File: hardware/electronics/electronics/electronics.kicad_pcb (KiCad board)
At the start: 2 copper layers, 130 x 100 mm, 14 parts, among them J1 Conn_Coaxial_Small, M1 Parachute_Servo, M2 Parachute_Servo, Q1 BC547, SW1 RBF, U1 RFM95W-915S2, U2 BMP585, U3 LSM6DS3, U4 SD Card mini module, U5 ESP32-S3-DEVKITC-1-N8R2, U6 GPS M8N, U7 MINI 560 STEP DOWN

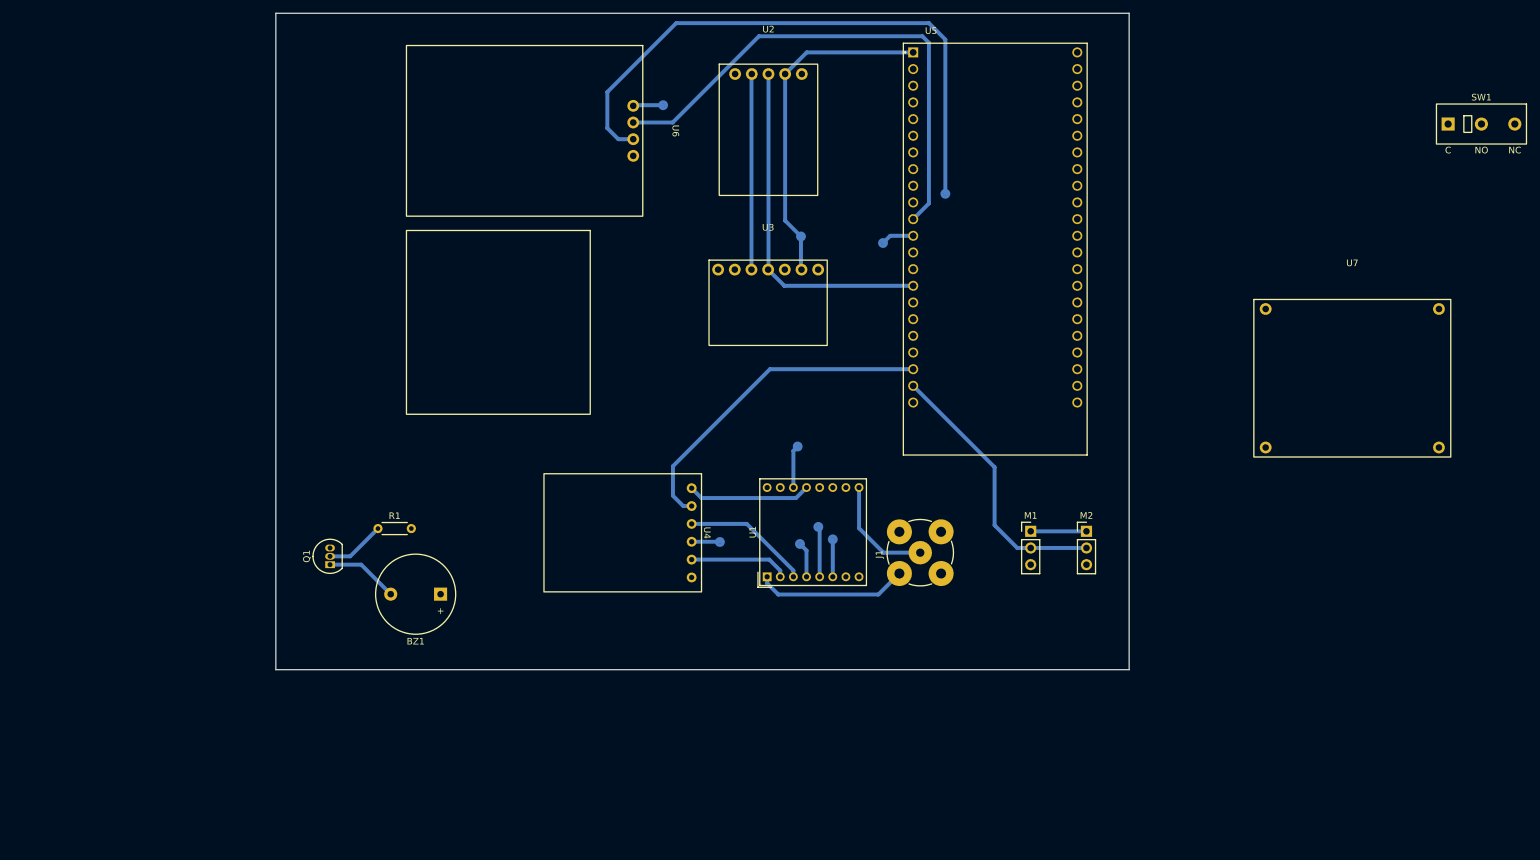
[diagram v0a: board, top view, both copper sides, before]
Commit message: Update flight-computer hardware files (PCB)
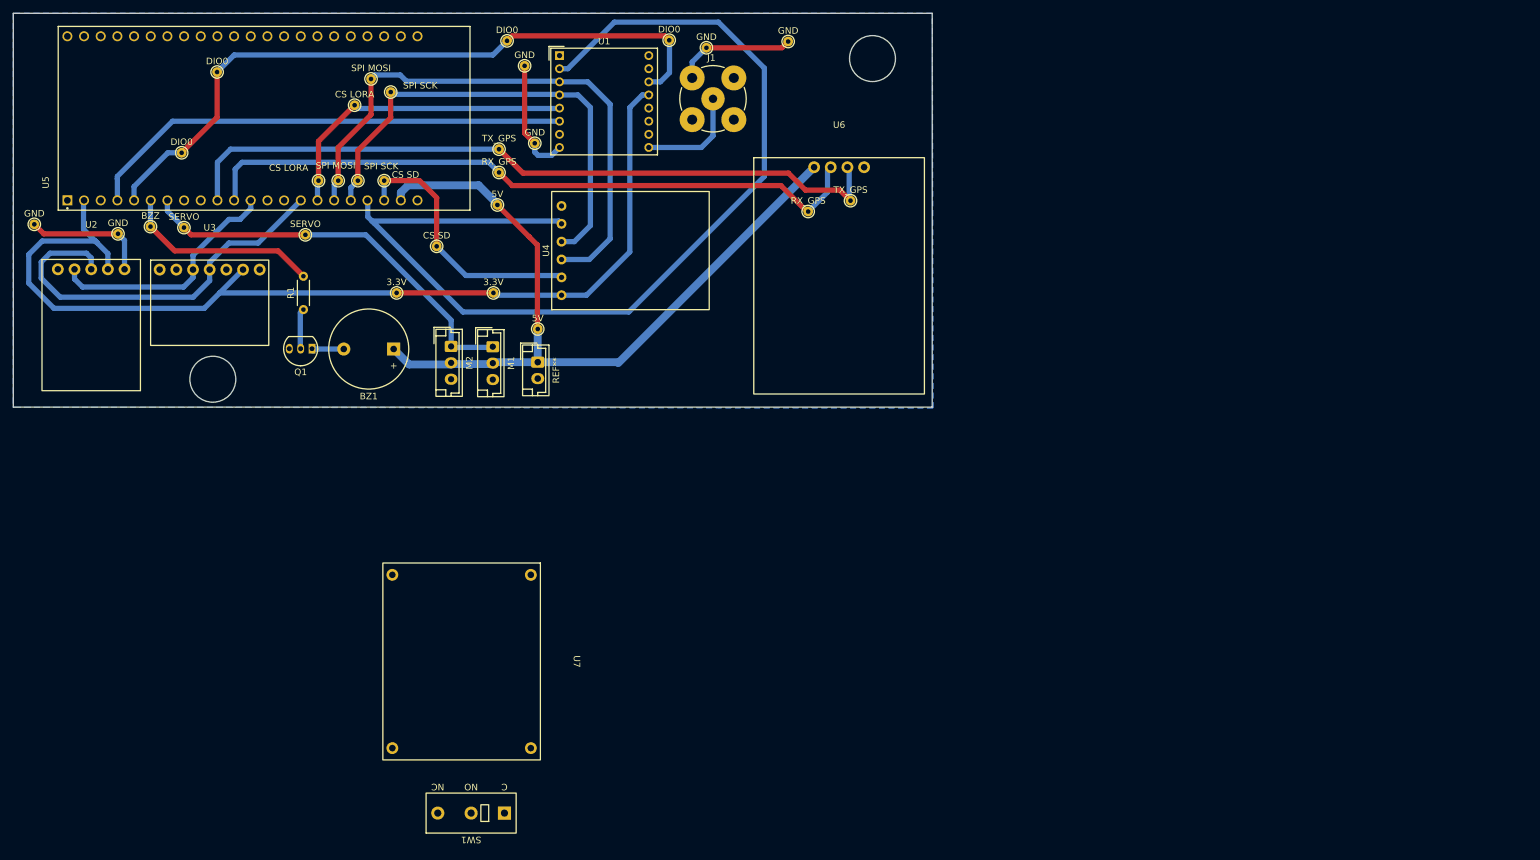
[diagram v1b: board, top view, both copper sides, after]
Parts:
- added 3.3V: TestPoint_THTPad_D1.5mm_Drill0.7mm, TestPoint:TestPoint_THTPad_D1.5mm_Drill0.7mm, F.Cu at (103.4, 92.6)
- added 3.3V: TestPoint_THTPad_D1.5mm_Drill0.7mm, TestPoint:TestPoint_THTPad_D1.5mm_Drill0.7mm, F.Cu at (118.2, 92.6)
- added 5V: TestPoint_THTPad_D1.5mm_Drill0.7mm, TestPoint:TestPoint_THTPad_D1.5mm_Drill0.7mm, F.Cu at (124.9, 98.1)
- added 5V: TestPoint_THTPad_D1.5mm_Drill0.7mm, TestPoint:TestPoint_THTPad_D1.5mm_Drill0.7mm, F.Cu at (118.8, 79.2)
- added BZZ: TestPoint_THTPad_D1.5mm_Drill0.7mm, TestPoint:TestPoint_THTPad_D1.5mm_Drill0.7mm, F.Cu at (65.9, 82.5)
- added CS LORA: TestPoint_THTPad_D1.5mm_Drill0.7mm, TestPoint:TestPoint_THTPad_D1.5mm_Drill0.7mm, F.Cu at (91.5, 75.5)
- added CS LORA: TestPoint_THTPad_D1.5mm_Drill0.7mm, TestPoint:TestPoint_THTPad_D1.5mm_Drill0.7mm, F.Cu at (97.0, 64.0)
- added CS SD: TestPoint_THTPad_D1.5mm_Drill0.7mm, TestPoint:TestPoint_THTPad_D1.5mm_Drill0.7mm, F.Cu at (101.5, 75.5)
- added CS SD: TestPoint_THTPad_D1.5mm_Drill0.7mm, TestPoint:TestPoint_THTPad_D1.5mm_Drill0.7mm, F.Cu at (109.5, 85.5)
- added DIO0: TestPoint_THTPad_D1.5mm_Drill0.7mm, TestPoint:TestPoint_THTPad_D1.5mm_Drill0.7mm, F.Cu at (76.0, 59.0)
- added DIO0: TestPoint_THTPad_D1.5mm_Drill0.7mm, TestPoint:TestPoint_THTPad_D1.5mm_Drill0.7mm, F.Cu at (120.2, 54.2)
- added DIO0: TestPoint_THTPad_D1.5mm_Drill0.7mm, TestPoint:TestPoint_THTPad_D1.5mm_Drill0.7mm, F.Cu at (70.7, 71.2)
- added DIO0: TestPoint_THTPad_D1.5mm_Drill0.7mm, TestPoint:TestPoint_THTPad_D1.5mm_Drill0.7mm, F.Cu at (144.9, 54.1)
- added GND: TestPoint_THTPad_D1.5mm_Drill0.7mm, TestPoint:TestPoint_THTPad_D1.5mm_Drill0.7mm, F.Cu at (163.1, 54.3)
- added GND: TestPoint_THTPad_D1.5mm_Drill0.7mm, TestPoint:TestPoint_THTPad_D1.5mm_Drill0.7mm, F.Cu at (124.5, 69.8)
- added GND: TestPoint_THTPad_D1.5mm_Drill0.7mm, TestPoint:TestPoint_THTPad_D1.5mm_Drill0.7mm, F.Cu at (61.0, 83.6)
- added GND: TestPoint_THTPad_D1.5mm_Drill0.7mm, TestPoint:TestPoint_THTPad_D1.5mm_Drill0.7mm, F.Cu at (122.9, 58.0)
- added GND: TestPoint_THTPad_D1.5mm_Drill0.7mm, TestPoint:TestPoint_THTPad_D1.5mm_Drill0.7mm, F.Cu at (150.6, 55.2)
- added GND: TestPoint_THTPad_D1.5mm_Drill0.7mm, TestPoint:TestPoint_THTPad_D1.5mm_Drill0.7mm, F.Cu at (48.2, 82.2)
- added REF**: JST_EH_B2B-EH-A_1x02_P2.50mm_Vertical, Connector_JST:JST_EH_B2B-EH-A_1x02_P2.50mm_Vertical, F.Cu at (124.9, 103.2)
- added RX_GPS: TestPoint_THTPad_D1.5mm_Drill0.7mm, TestPoint:TestPoint_THTPad_D1.5mm_Drill0.7mm, F.Cu at (166.1, 80.2)
- added RX_GPS: TestPoint_THTPad_D1.5mm_Drill0.7mm, TestPoint:TestPoint_THTPad_D1.5mm_Drill0.7mm, F.Cu at (119.0, 74.2)
- added SERVO: TestPoint_THTPad_D1.5mm_Drill0.7mm, TestPoint:TestPoint_THTPad_D1.5mm_Drill0.7mm, F.Cu at (71.0, 82.7)
- added SERVO: TestPoint_THTPad_D1.5mm_Drill0.7mm, TestPoint:TestPoint_THTPad_D1.5mm_Drill0.7mm, F.Cu at (89.5, 83.8)
- added SPI MOSI: TestPoint_THTPad_D1.5mm_Drill0.7mm, TestPoint:TestPoint_THTPad_D1.5mm_Drill0.7mm, F.Cu at (94.5, 75.5)
- added SPI MOSI: TestPoint_THTPad_D1.5mm_Drill0.7mm, TestPoint:TestPoint_THTPad_D1.5mm_Drill0.7mm, F.Cu at (99.5, 60.0)
- added SPI SCK: TestPoint_THTPad_D1.5mm_Drill0.7mm, TestPoint:TestPoint_THTPad_D1.5mm_Drill0.7mm, F.Cu at (97.5, 75.5)
- added SPI SCK: TestPoint_THTPad_D1.5mm_Drill0.7mm, TestPoint:TestPoint_THTPad_D1.5mm_Drill0.7mm, F.Cu at (102.5, 62.0)
- added TX_GPS: TestPoint_THTPad_D1.5mm_Drill0.7mm, TestPoint:TestPoint_THTPad_D1.5mm_Drill0.7mm, F.Cu at (172.6, 78.5)
- added TX_GPS: TestPoint_THTPad_D1.5mm_Drill0.7mm, TestPoint:TestPoint_THTPad_D1.5mm_Drill0.7mm, F.Cu at (119.0, 70.7)
- M1, M2: footprint Connector_PinHeader_2.54mm:PinHeader_1x03_P2.54mm_Vertical -> Connector_JST:JST_EH_B3B-EH-A_1x03_P2.50mm_Vertical
- moved SW1 178.0 mm to (119.8, 171.8), turned to 180 degrees
- moved U7 135.4 mm to (125.3, 148.8), turned to -90 degrees
- moved U5 113.2 mm to (83.2, 66.0), turned to 90 degrees
- moved U2 107.4 mm to (56.9, 87.5)
- moved M2 100.8 mm to (111.7, 100.8), turned to -90 degrees
- moved M1 86.6 mm to (118.0, 100.8), turned to -90 degrees
- moved U1 85.5 mm to (128.2, 56.4), turned to 0 degrees
- moved U3 85.1 mm to (74.9, 87.6)
- moved J1 76.0 mm to (151.6, 63.0), turned to 0 degrees
- moved U4 48.7 mm to (127.0, 86.2), turned to 90 degrees
- moved BZ1 38.0 mm to (103.0, 101.2)
- moved R1 35.2 mm to (89.2, 95.1), turned to 90 degrees
- moved Q1 33.1 mm to (90.0, 101.1), turned to 180 degrees
- moved U6 30.2 mm to (170.8, 72.0), turned to 0 degrees
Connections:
- J1 pad 2: Net-(J1-Ext) -> /GND
- U1 pad 1: Net-(J1-Ext) -> /GND
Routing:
- net /MISO: track 15.1 -> 160.5 mm
- net /LORA_DIO0: track 6.52 -> 105.1 mm
- net /3.3 VCC: track 70.5 -> 155.5 mm
- net /5 VCC: track 46.4 -> 121.8 mm
- net /MOSI: track 19.4 -> 88.6 mm
- net /LORA_RESET: track 5.70 -> 74.5 mm
- net /SCK: track 9.75 -> 74.0 mm
- net /GND: track 0.00 -> 55.8 mm
- net /SERVO: track 8.50 -> 61.1 mm
- net /SPI_CS_LORA: track 7.68 -> 48.3 mm
- net /BZZ: track 0.00 -> 30.4 mm
- net /RX_GPS: track 78.8 -> 103.3 mm
- net Net-(J1-Ext): track 23.2 -> 0.00 mm
- net /TX_GPS: track 90.5 -> 111.6 mm
- net /CS_SD: track 50.7 -> 39.8 mm
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- added copper zone on B.Cu, net /GND
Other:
- board size 130 x 100 mm -> 140 x 60 mm
